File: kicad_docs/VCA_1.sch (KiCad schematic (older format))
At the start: 16 parts, among them U1 SSM2164, U2 TL072, U3 TL072, U4 TL072

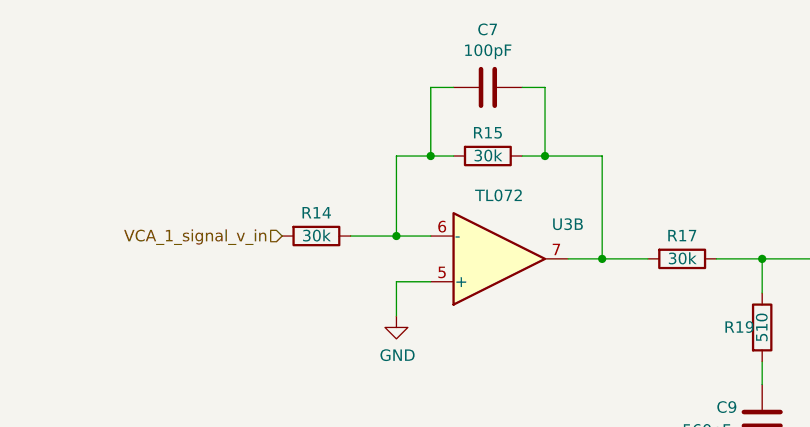
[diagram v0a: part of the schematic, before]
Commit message: add AC/DC coupling caps and jumper
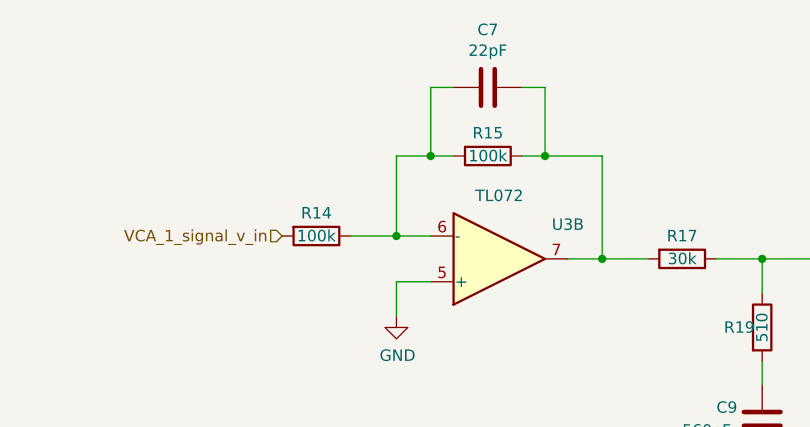
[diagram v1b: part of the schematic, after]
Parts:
- C7: value 100pF -> 22pF
- R14, R15: value 30k -> 100k
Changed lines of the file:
@@
 AR Path="/5E4A03B7/5E9B018F" Ref="R?"  Part="1"
 F 0 "R15" V 4950 2150 50  0000 C CNN
-F 1 "30k" V 5050 2150 50  0000 C CNN
+F 1 "100k" V 5050 2150 50  0000 C CNN
 F 2 "Resistor_SMD:R_0805_2012Metric_Pad1.15x1.40mm_HandSolder" V 4980 2150 50  0001 C CNN
 F 3 "~" H 5050 2150 50  0001 C CNN
@@
 AR Path="/5E4A03B7/5E9B01A7" Ref="R?"  Part="1"
 F 0 "R14" V 4200 2500 50  0000 C CNN
-F 1 "30k" V 4300 2500 50  0000 C CNN
+F 1 "100k" V 4300 2500 50  0000 C CNN
 F 2 "Resistor_SMD:R_0805_2012Metric_Pad1.15x1.40mm_HandSolder" V 4230 2500 50  0001 C CNN
 F 3 "~" H 4300 2500 50  0001 C CNN
@@
 AR Path="/5E4A03B7/5E9B01BB" Ref="C?"  Part="1"
 F 0 "C7" V 4798 1850 50  0000 C CNN
-F 1 "100pF" V 4889 1850 50  0000 C CNN
+F 1 "22pF" V 4889 1850 50  0000 C CNN
 F 2 "Capacitor_SMD:C_0805_2012Metric_Pad1.15x1.40mm_HandSolder" H 5088 1700 50  0001 C CNN
 F 3 "~" H 5050 1850 50  0001 C CNN

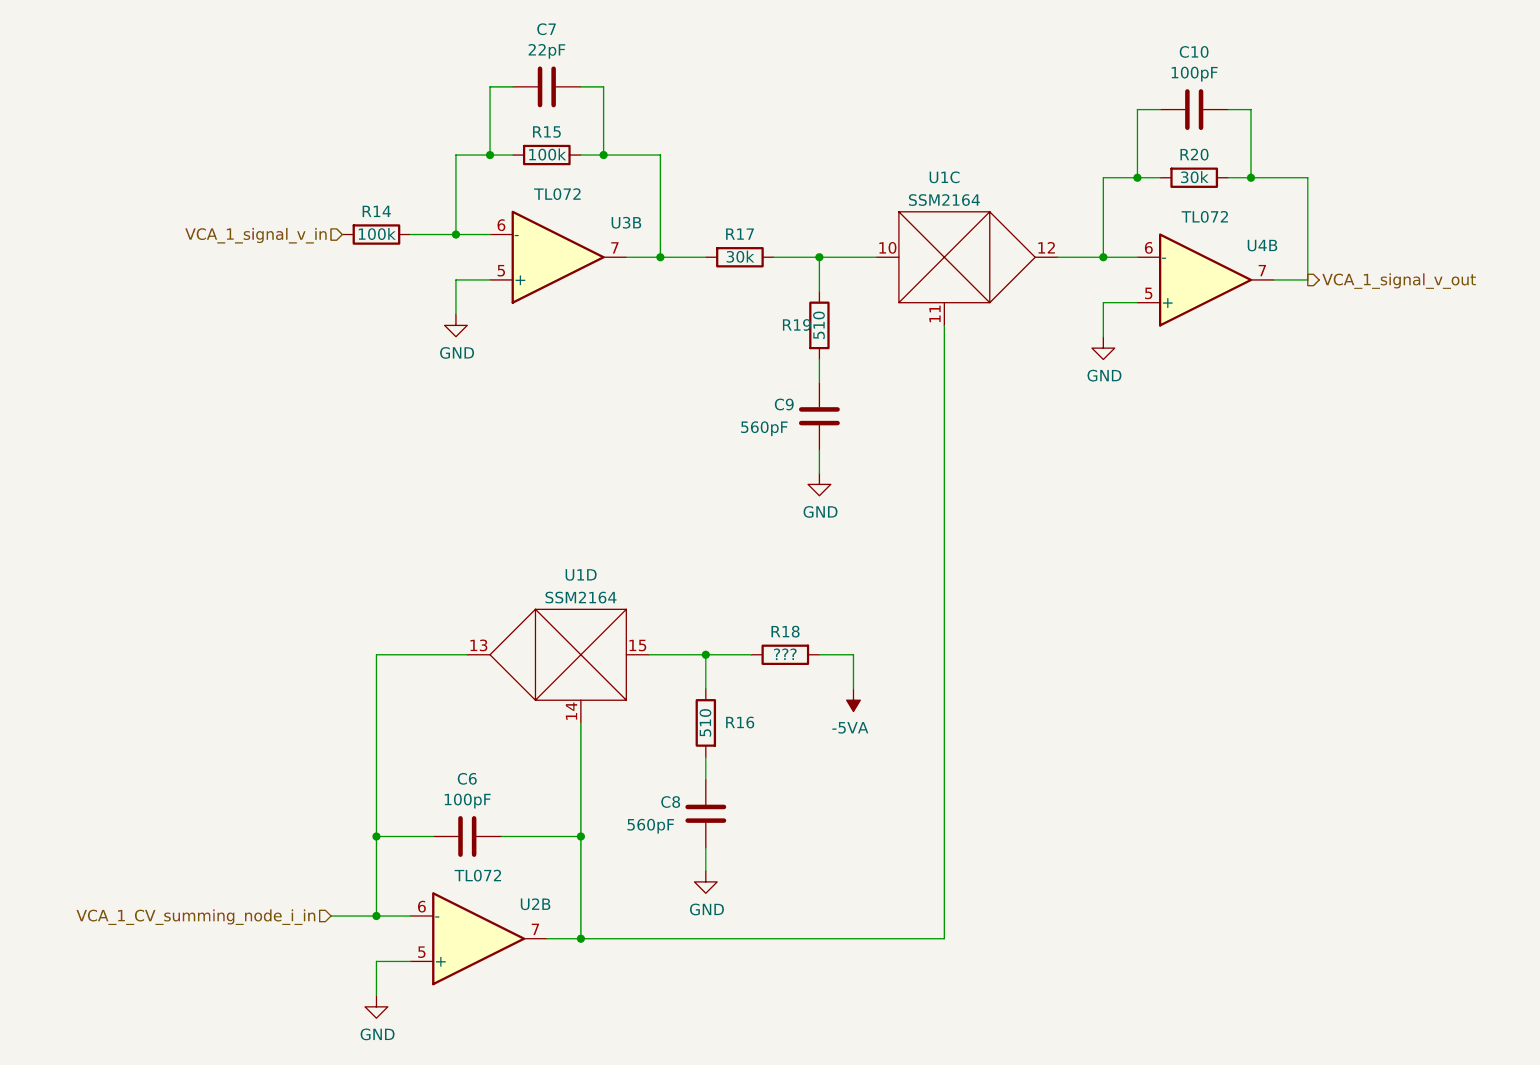
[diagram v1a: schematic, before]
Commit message: add values to r's, add r's to CV circuit
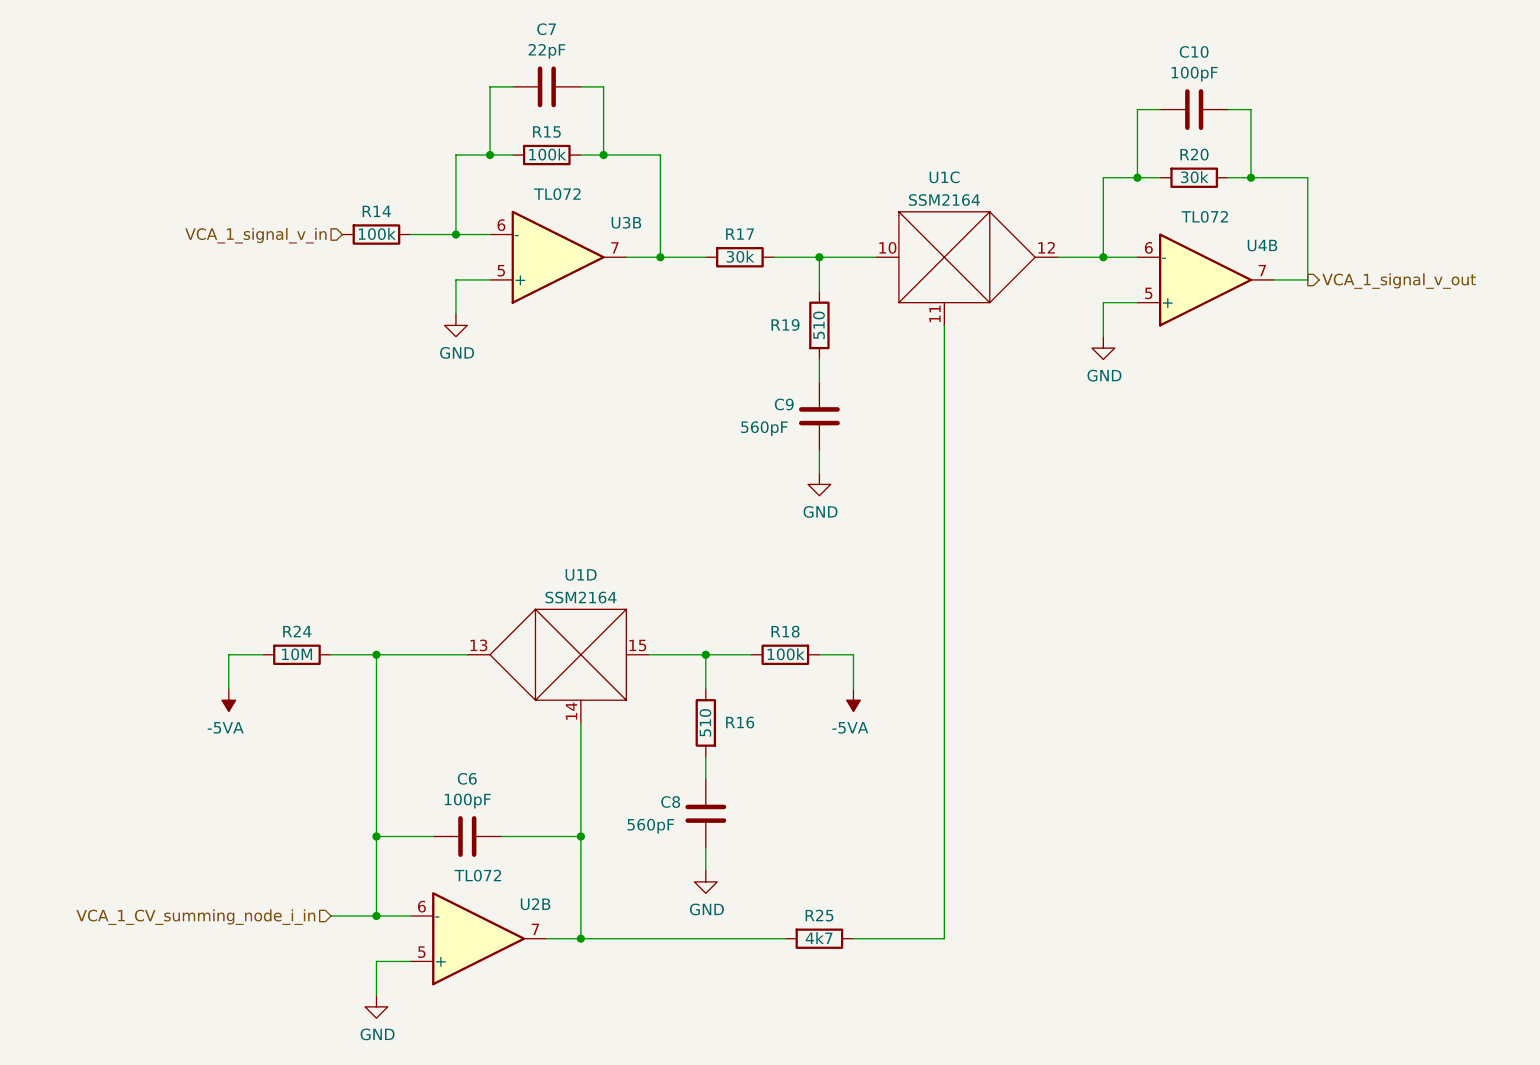
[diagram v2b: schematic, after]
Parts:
- added R24: 10M, Resistor_SMD:R_0805_2012Metric_Pad1.15x1.40mm_HandSolder, symbol Device:R
- added R25: 4k7, Resistor_SMD:R_0805_2012Metric_Pad1.15x1.40mm_HandSolder, symbol Device:R
- R18: value ??? -> 100k
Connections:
- net -5VA: now also R24.2
- net VCA_1_CV_summing_node_i_in: now also R24.1
- net at C6.1, U1.14, U2.7: now also R25.2; no longer U1.11
- new net: R25.1, U1.11
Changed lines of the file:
@@
 AR Path="/5E4A0387/5E9B011E" Ref="R?"  Part="1"
 AR Path="/5E4A03B7/5E9B011E" Ref="R?"  Part="1"
-F 0 "R19" H 6150 2900 50  0000 C CNN
+F 0 "R19" H 6100 2900 50  0000 C CNN
 F 1 "510" V 6250 2900 50  0000 C CNN
 F 2 "Resistor_SMD:R_0805_2012Metric_Pad1.15x1.40mm_HandSolder" V 6180 2900 50  0001 C CNN
@@
 	5750 4900 5750 4800
 Wire Wire Line
-	5200 5600 6800 5600
-Wire Wire Line
 	6800 5600 6800 2900
-Connection ~ 5200 5600
 $Comp
 L Amplifier_Operational:TL072 U?
@@
 AR Path="/5E4A03B7/5E9B01C9" Ref="R?"  Part="1"
 F 0 "R18" V 6000 4350 50  0000 C CNN
-F 1 "???" V 6100 4350 50  0000 C CNN
+F 1 "100k" V 6100 4350 50  0000 C CNN
 F 2 "Resistor_SMD:R_0805_2012Metric_Pad1.15x1.40mm_HandSolder" V 6030 4350 50  0001 C CNN
 F 3 "~" H 6100 4350 50  0001 C CNN
@@
 	6400 4350 6250 4350
 Connection ~ 5750 4350
+$Comp
+L Device:R R25
+U 1 1 5E4607C4
+P 6250 5600
+F 0 "R25" V 6150 5600 50  0000 C CNN
+F 1 "4k7" V 6250 5600 50  0000 C CNN
+F 2 "Resistor_SMD:R_0805_2012Metric_Pad1.15x1.40mm_HandSolder" V 6180 5600 50  0001 C CNN
+F 3 "~" H 6250 5600 50  0001 C CNN
+	1    6250 5600
+	0    1    1    0
+$EndComp
+Wire Wire Line
+	6800 5600 6400 5600
+Wire Wire Line
+	6100 5600 5200 5600
+Connection ~ 5200 5600
+$Comp
+L Device:R R24
+U 1 1 5E468B49
+P 3950 4350
+F 0 "R24" V 3850 4350 50  0000 C CNN
+F 1 "10M" V 3950 4350 50  0000 C CNN
+F 2 "Resistor_SMD:R_0805_2012Metric_Pad1.15x1.40mm_HandSolder" V 3880 4350 50  0001 C CNN
+F 3 "~" H 3950 4350 50  0001 C CNN
+	1    3950 4350
+	0    1    1    0
+$EndComp
+$Comp
+L power:-5VA #PWR015
+U 1 1 5E46CA7E
+P 3650 4500
+AR Path="/5E48E312/5E46CA7E" Ref="#PWR015"  Part="1"
+AR Path="/5E4A03B7/5E46CA7E" Ref="#PWR?"  Part="1"
+F 0 "#PWR015" H 3650 4600 50  0001 C CNN
+F 1 "-5VA" H 3665 4673 50  0000 C CNN
+F 2 "" H 3650 4500 50  0001 C CNN
+F 3 "" H 3650 4500 50  0001 C CNN
+	1    3650 4500
+	-1   0    0    1
+$EndComp
+Wire Wire Line
+	3650 4500 3650 4350
+Wire Wire Line
+	3650 4350 3800 4350
+Wire Wire Line
+	4100 4350 4300 4350
+Connection ~ 4300 4350
 $EndSCHEMATC
